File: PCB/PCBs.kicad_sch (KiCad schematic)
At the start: 8 parts, among them U1 ADS1299IPAGR

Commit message: dvdd clk and clksel
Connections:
- net at U2.21 (GP16): now also U1.34 (DIN)
- net at U2.22 (GP17): now also U1.39 (*CS)
- net at U2.24 (GP18): now also U1.40 (SCLK)
- net at U2.25 (GP19): now also U1.43 (DOUT)
- net DVDD: now reaches U1.48 (DVDD)
- net DVDD: now also U1.50 (DVDD), U1.52 (CLKSEL)
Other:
- note added: "TODO: pull up resistor?"
- moved on the sheet: U2

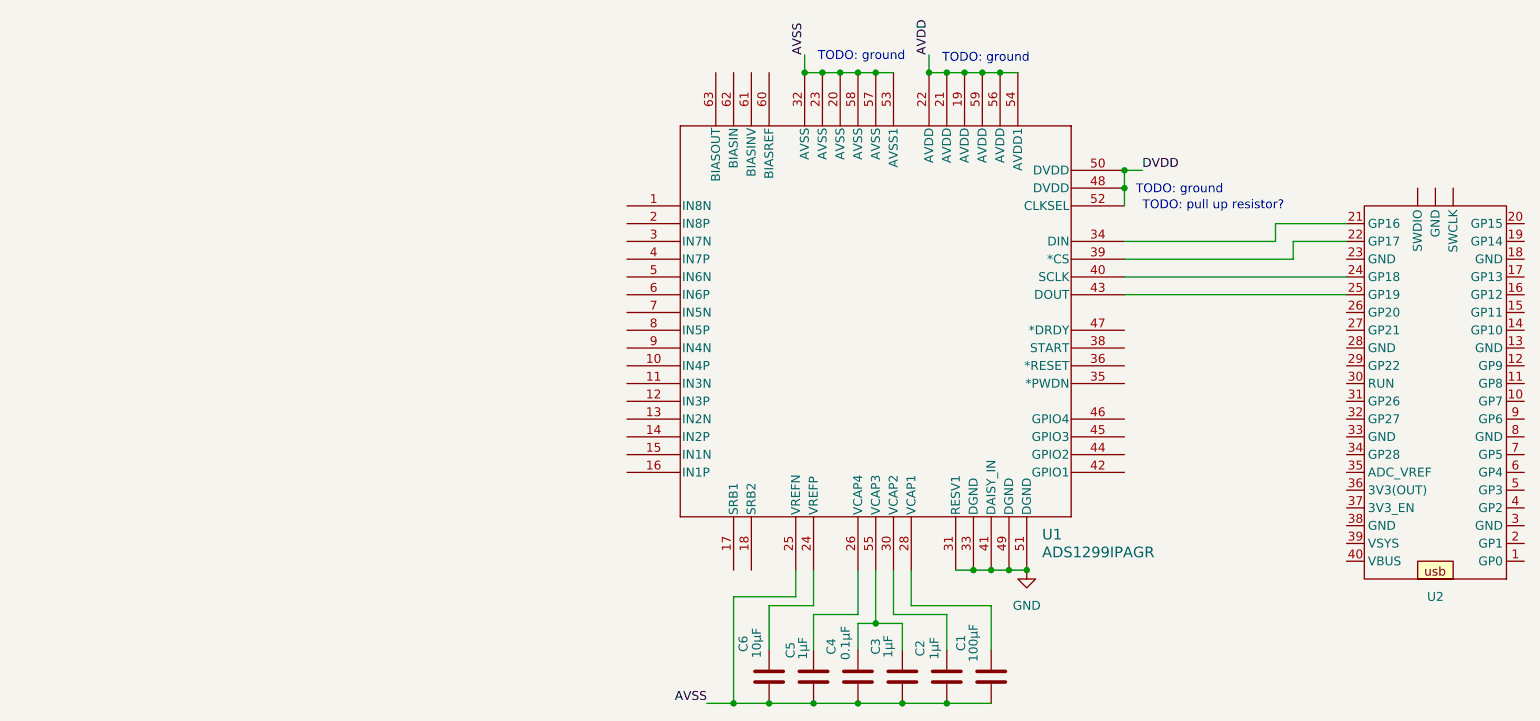
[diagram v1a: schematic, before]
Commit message: first input schem draft
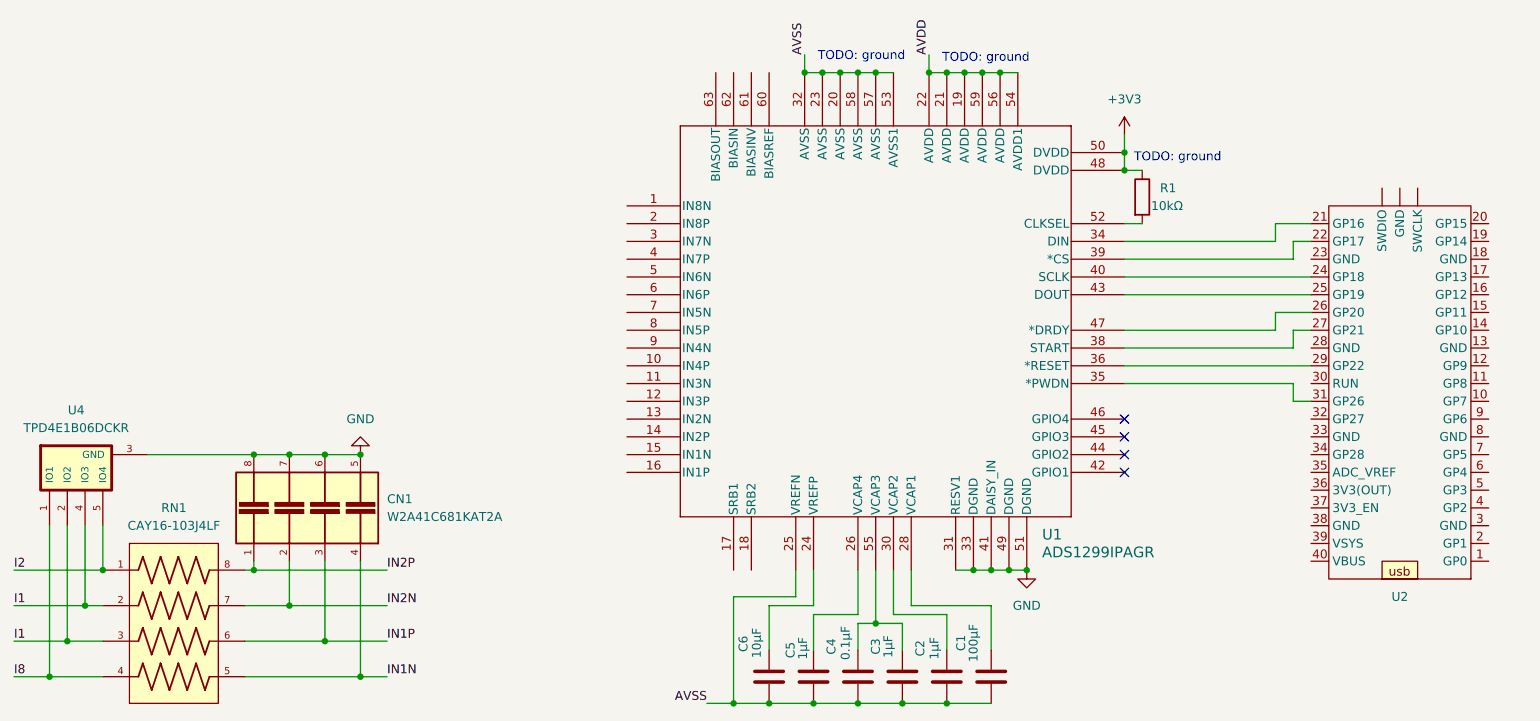
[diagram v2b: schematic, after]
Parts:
- added CN1: W2A41C681KAT2A, W2A41C681KAT2A:CAPCAXE50P210X130X94-8N, symbol custom_lib:W2A41C681KAT2A
- added R1: 10kΩ, symbol Device:R
- added RN1: CAY16-103J4LF, CAY16-103J4LF:RESCAF80P320X160X60-8N, symbol custom_lib:CAY16-103J4LF
- added U4: TPD4E1B06DCKR, TPD4E1B06DCKR:SOT65P210X110-6N, symbol custom_lib:TPD4E1B06DCKR
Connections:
- net GND: now also CN1.5, CN1.6, CN1.7, CN1.8, U4.3 (GND)
- net at U2.26 (GP20): now also U1.47 (*DRDY)
- net at U2.27 (GP21): now also U1.38 (START)
- net at U2.29 (GP22): now also U1.36 (*RESET)
- net at U2.31 (GP26): now also U1.35 (*PWDN)
- net DVDD renamed +3V3
- net +3V3: now also R1.1; no longer U1.52 (CLKSEL)
- new net: R1.2, U1.52 (CLKSEL)
- new net I1: RN1.2, RN1.3, U4.2 (IO2), U4.4 (IO3)
- new net I2: RN1.1, U4.5 (IO4)
- new net I8: RN1.4, U4.1 (IO1)
- new net IN1N: CN1.4, RN1.5
- new net IN1P: CN1.3, RN1.6
- new net IN2N: CN1.2, RN1.7
- new net IN2P: CN1.1, RN1.8
- no-connect marks 0 -> 4
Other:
- note removed: "TODO: pull up resistor?"
- moved on the sheet: U2

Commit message: input cp
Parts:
- added CN2, CN3, CN4: W2A41C681KAT2A, W2A41C681KAT2A:CAPCAXE50P210X130X94-8N, symbol custom_lib:W2A41C681KAT2A
- added RN2, RN3, RN4: CAY16-103J4LF, CAY16-103J4LF:RESCAF80P320X160X60-8N, symbol custom_lib:CAY16-103J4LF
- added U3, U5, U6: TPD4E1B06DCKR, TPD4E1B06DCKR:SOT65P210X110-6N, symbol custom_lib:TPD4E1B06DCKR
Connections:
- net GND: now also CN2.5, CN2.6, CN2.7, CN2.8, CN3.5, CN3.6, CN3.7, CN3.8, CN4.5, CN4.6, CN4.7, CN4.8, U3.3 (GND), U5.3 (GND), U6.3 (GND)
- net I2: now also RN2.4, U3.1 (IO1)
- net I8: now also RN4.1, U6.5 (IO4)
- new net I3: RN2.2, RN2.3, U3.2 (IO2), U3.4 (IO3)
- new net I4: RN2.1, RN3.4, U3.5 (IO4), U5.1 (IO1)
- new net I5: RN3.2, RN3.3, U5.2 (IO2), U5.4 (IO3)
- new net I6: RN3.1, RN4.4, U5.5 (IO4), U6.1 (IO1)
- new net I7: RN4.2, RN4.3, U6.2 (IO2), U6.4 (IO3)
- new net IN3N: CN2.4, RN2.5
- new net IN3P: CN2.3, RN2.6
- new net IN4N: CN2.2, RN2.7
- new net IN4P: CN2.1, RN2.8
- new net IN5N: CN3.4, RN3.5
- new net IN5P: CN3.3, RN3.6
- new net IN6N: CN3.2, RN3.7
- new net IN6P: CN3.1, RN3.8
- new net IN7N: CN4.4, RN4.5
- new net IN7P: CN4.3, RN4.6
- new net IN8N: CN4.2, RN4.7
- new net IN8P: CN4.1, RN4.8
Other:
- moved on the sheet: C1, C2, C3, C4, C5, C6, CN1, R1, RN1, U1, U2, U4

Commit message: input offset montage
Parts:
- removed U3: TPD4E1B06DCKR, TPD4E1B06DCKR:SOT65P210X110-6N, symbol custom_lib:TPD4E1B06DCKR
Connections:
- net GND: now also CN2.1, CN2.2, CN2.3, CN2.4; no longer CN2.5, CN2.6, CN2.7, CN2.8
- net I1: no longer U4.2 (IO2)
- net I2: now also U4.2 (IO2); no longer U4.5 (IO4)
- net I3: now also U4.1 (IO1)
- net I8: now also U4.5 (IO4); no longer U4.1 (IO1)
- net IN3N: now also CN2.8; no longer CN2.4
- net IN3P: now also CN2.7; no longer CN2.3
- net IN4N: now also CN2.6; no longer CN2.2
- net IN4P: now also CN2.5; no longer CN2.1
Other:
- moved on the sheet: CN1, CN2, CN3, CN4, RN1, RN2, RN3, RN4, U5, U6

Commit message: duplicate input
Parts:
- removed CN3: W2A41C681KAT2A, W2A41C681KAT2A:CAPCAXE50P210X130X94-8N, symbol custom_lib:W2A41C681KAT2A
- removed RN3: CAY16-103J4LF, CAY16-103J4LF:RESCAF80P320X160X60-8N, symbol custom_lib:CAY16-103J4LF
- removed U5: TPD4E1B06DCKR, TPD4E1B06DCKR:SOT65P210X110-6N, symbol custom_lib:TPD4E1B06DCKR
- added CN5, CN6: W2A41C681KAT2A, W2A41C681KAT2A:CAPCAXE50P210X130X94-8N, symbol custom_lib:W2A41C681KAT2A
- added RN5, RN6: CAY16-103J4LF, CAY16-103J4LF:RESCAF80P320X160X60-8N, symbol custom_lib:CAY16-103J4LF
- added U3: TPD4E1B06DCKR, TPD4E1B06DCKR:SOT65P210X110-6N, symbol custom_lib:TPD4E1B06DCKR
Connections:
- net GND: now also CN5.1, CN5.2, CN5.3, CN5.4, CN6.5, CN6.6, CN6.7, CN6.8, U3.3 (GND)
- net I4: now also RN6.4, U3.5 (IO4)
- net I5: now also RN6.2, RN6.3, U3.4 (IO3)
- net I6: now also RN5.4, RN6.1, U3.2 (IO2)
- net I7: now also RN5.2, RN5.3, U3.1 (IO1)
- net I8: now also RN5.1
- net IN5N: now also CN6.4, RN6.5
- net IN5P: now also CN6.3, RN6.6
- net IN6N: now also CN6.2, RN6.7
- net IN6P: now also CN6.1, RN6.8
- net IN7N: now also CN5.8, RN5.5
- net IN7P: now also CN5.7, RN5.6
- net IN8N: now also CN5.6, RN5.7
- net IN8P: now also CN5.5, RN5.8
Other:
- moved on the sheet: CN1, CN2, CN4, RN1, RN2, RN4, U4, U6

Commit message: bias input draft
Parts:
- removed CN5: W2A41C681KAT2A, W2A41C681KAT2A:CAPCAXE50P210X130X94-8N, symbol custom_lib:W2A41C681KAT2A
- added C7: C, symbol Device:C
- added C8: 1.5nF, symbol Device:C
- added CN3: W2A41C681KAT2A, W2A41C681KAT2A:CAPCAXE50P210X130X94-8N, symbol custom_lib:W2A41C681KAT2A
- added D1: TPD1E05U06DPYR, TPD1E05U06DPYR:DIO_TPD1E05U06DPYR, symbol custom_lib:TPD1E05U06DPYR
- added R2: R, symbol Device:R
- added R3: 1MΩ, symbol Device:R
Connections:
- net AVSS: now also U1.17 (SRB1), U1.18 (SRB2), U1.60 (BIASREF)
- net GND: now also C7.1, CN3.1, CN3.2, CN3.3, CN3.4, D1.2 (GND)
- net IN1N: now also U1.15 (IN1N)
- net IN1P: now also U1.16 (IN1P)
- net IN2N: now also U1.13 (IN2N)
- net IN2P: now also U1.14 (IN2P)
- net IN3N: now also U1.11 (IN3N)
- net IN3P: now also U1.12 (IN3P)
- net IN4N: now also U1.9 (IN4N)
- net IN4P: now also U1.10 (IN4P)
- net IN5N: now also U1.7 (IN5N)
- net IN5P: now also U1.8 (IN5P)
- net IN6N: now also U1.5 (IN6N)
- net IN6P: now also U1.6 (IN6P)
- net IN7N: now also U1.3 (IN7N), CN3.8
- net IN7P: now also U1.4 (IN7P), CN3.7
- net IN8N: now also U1.1 (IN8N), CN3.6
- net IN8P: now also U1.2 (IN8P), CN3.5
- net at U1.61 (BIASINV): now also C8.1, R3.1
- net Bias: now reaches U1.62 (BIASIN)
- net Bias: now also U1.63 (BIASOUT), C7.2, C8.2, R2.1, R3.2
- new net IB: D1.1 (I/O), R2.2
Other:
- note added: "TODO: AVSS or GND?"
- moved on the sheet: C1, C2, C3, C4, C5, C6, CN1, CN2, CN6, R1, RN1, RN2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

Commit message: volt regs
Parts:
- added U5: TPS73225DBVR, TPS73225DBVR:SOT95P280X145-5N, symbol custom_lib:TPS73225DBVR
- added U7: LM2664M6, LM2664M6:SOT95P300X120-6N, symbol custom_lib:LM2664M6
- added U8: TPS73233DBVT, TPS73233DBVT:SOT95P280X145-5N, symbol custom_lib:TPS73233DBVT
- added U9: TPS72325DBVT, TPS72325DBVT:SOT95P280X145-5N, symbol custom_lib:TPS72325DBVT
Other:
- note added: "TODO: +0.1uF"
- note added: "TODO: GND P64"
- note added: "TODO: pull resistors"
- note added: "TODO: verify"

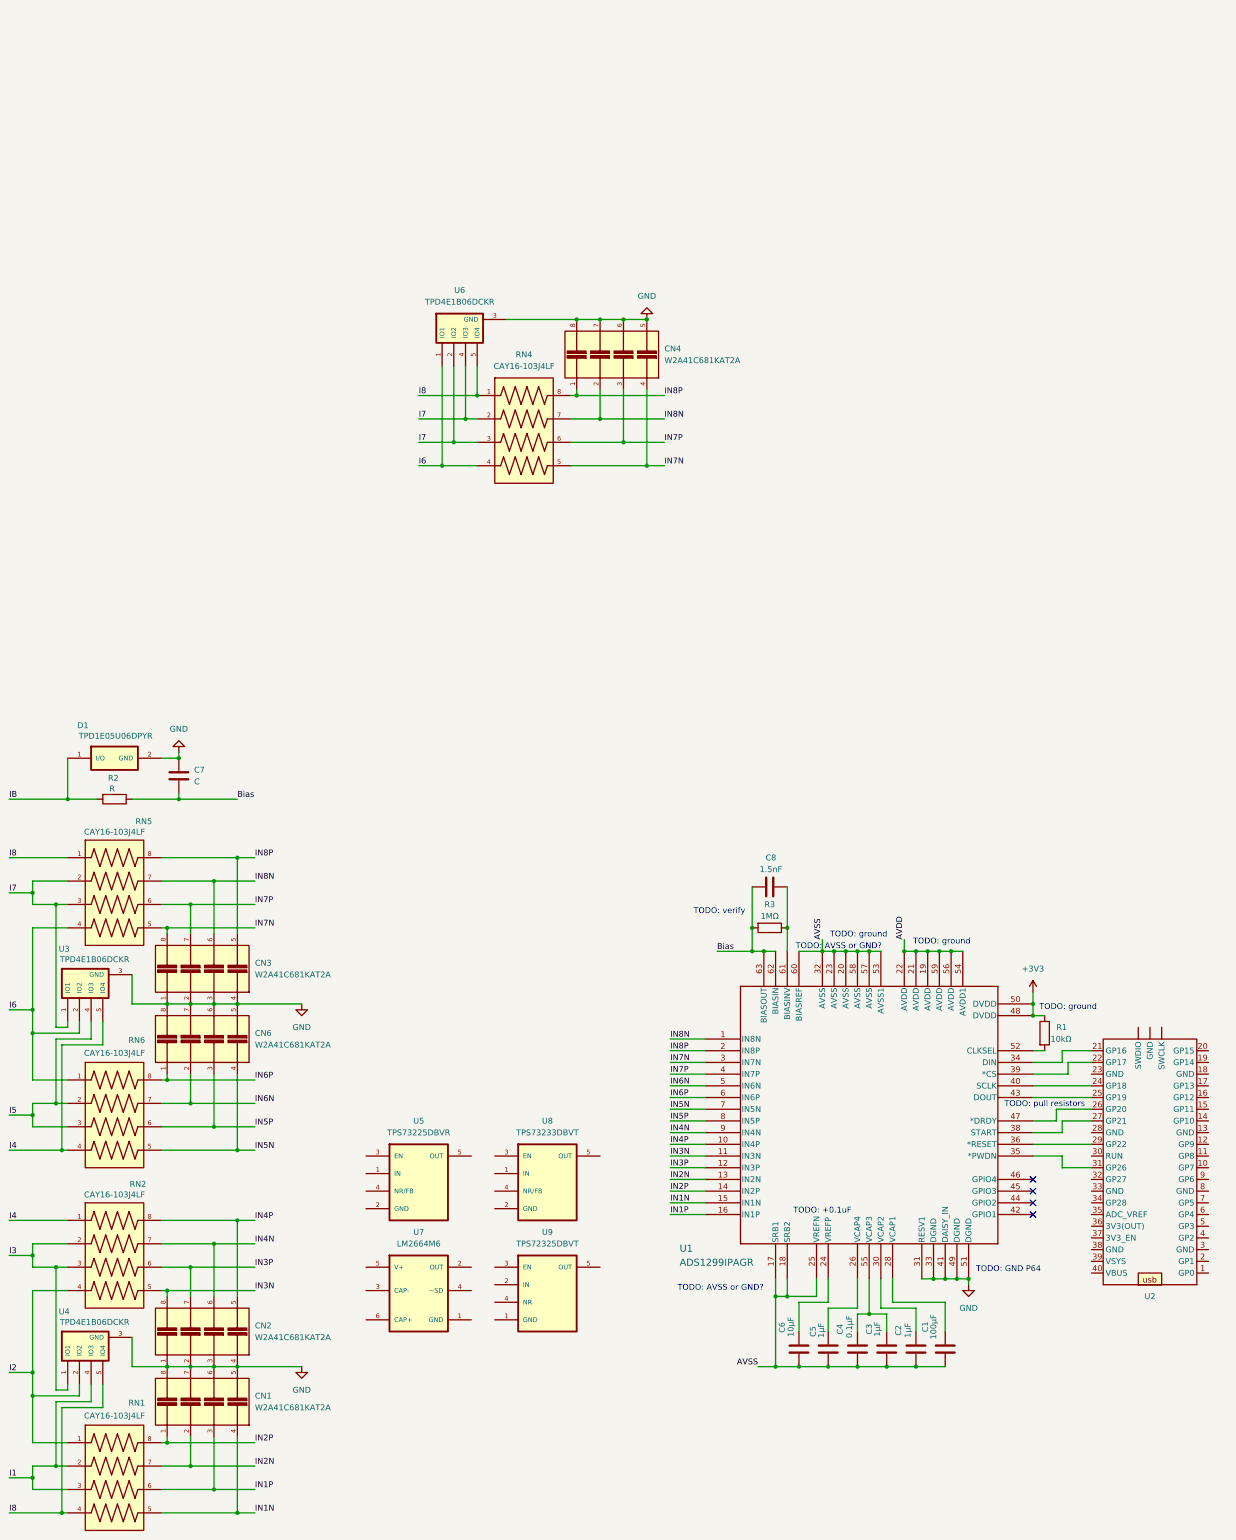
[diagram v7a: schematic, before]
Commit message: booster and voltage regulators
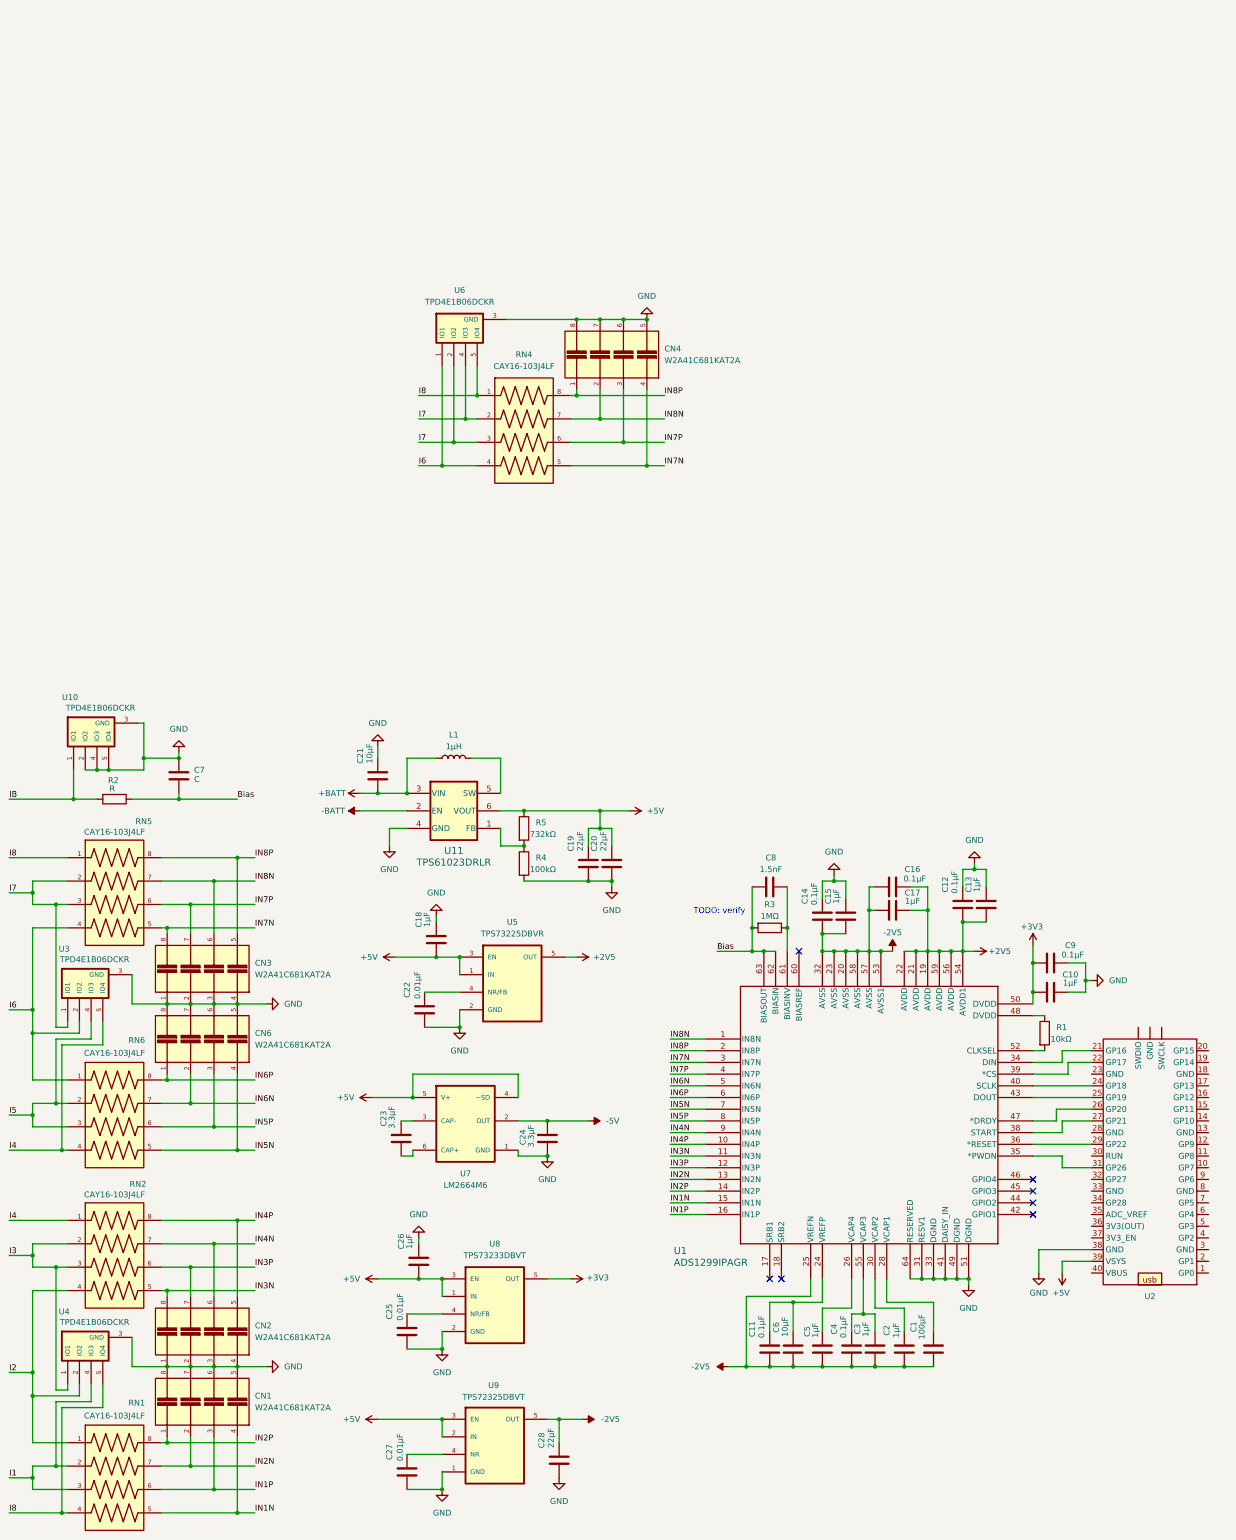
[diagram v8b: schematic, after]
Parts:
- removed D1: TPD1E05U06DPYR, TPD1E05U06DPYR:DIO_TPD1E05U06DPYR, symbol custom_lib:TPD1E05U06DPYR
- added C10, C13, C15, C17, C18, C26: 1µF, symbol Device:C
- added C11, C12, C14, C16, C9: 0.1µF, symbol Device:C
- added C19, C20, C28: 22µF, symbol Device:C
- added C21: 10µF, symbol Device:C
- added C22, C25, C27: 0.01µF, symbol Device:C
- added C23, C24: 3.3µF, symbol Device:C
- added L1: 1µH, symbol Device:L
- added R4: 100kΩ, symbol Device:R
- added R5: 732kΩ, symbol Device:R
- added U10: TPD4E1B06DCKR, TPD4E1B06DCKR:SOT65P210X110-6N, symbol custom_lib:TPD4E1B06DCKR
- added U11: TPS61023DRLR, DRL0006A, symbol custom_lib:TPS61023DRLR
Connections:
- net AVDD is gone; now on net +2V5: U1.19 (AVDD), U1.21 (AVDD), U1.22 (AVDD), U1.54 (AVDD1), U1.56 (AVDD), U1.59 (AVDD)
- net +3V3: now also U8.5 (OUT), C10.1, C9.1; no longer R1.1, U1.48 (DVDD)
- net GND: now also U1.64 (RESERVED), U2.38 (GND), U5.2 (GND), U7.1 (GND), U8.2 (GND), U9.1 (GND), C10.2, C12.2, C13.2, C14.2, C15.2, C18.2, C19.1, C20.1, C21.2, C22.1, C24.1, C25.1, C26.2, C27.1, C28.1, C9.2, R4.2, U10.2 (IO2), U10.3 (GND), U10.4 (IO3), U10.5 (IO4), U11.4 (GND)
- net IB: now also U10.1 (IO1)
- net +5V: now reaches U9.2 (IN)
- net +5V: now also U2.39 (VSYS), U5.1 (IN), U5.3 (EN), U7.4 (~SD), U7.5 (V+), U8.1 (IN), U8.3 (EN), U9.3 (EN), C18.1, C19.2, C20.2, C26.1, R5.1, U11.6 (VOUT)
- net at U9.4 (NR): now also C27.2
- net -2V5: now reaches U9.5 (OUT)
- net -2V5: now also C1.2, C2.2, C3.1, C4.1, C5.2, C6.2, U1.20 (AVSS), U1.23 (AVSS), U1.25 (VREFN), U1.32 (AVSS), U1.53 (AVSS1), U1.57 (AVSS), U1.58 (AVSS), C11.1, C14.1, C15.1, C16.1, C17.1, C28.2
- net at U5.4 (NR/FB): now also C22.2
- net +2V5: now reaches U5.5 (OUT)
- net +2V5: now also C12.1, C13.1, C16.2, C17.2
- net -5V: now reaches U7.2 (OUT)
- net -5V: now also C24.2
- net at U7.3 (CAP-): now also C23.2
- net at U7.6 (CAP+): now also C23.1
- net at U8.4 (NR/FB): now also C25.2
- net at C6.1, U1.24 (VREFP): now also C11.2
- removed net AVSS: C1.2, C2.2, C3.1, C4.1, C5.2, C6.2, U1.17 (SRB1), U1.18 (SRB2), U1.20 (AVSS), U1.23 (AVSS), U1.25 (VREFN), U1.32 (AVSS), U1.53 (AVSS1), U1.57 (AVSS), U1.58 (AVSS), U1.60 (BIASREF)
- new net: L1.2, U11.5 (SW)
- new net: R4.1, R5.2, U11.1 (FB)
- new net: R1.1, U1.48 (DVDD)
- new net +BATT: C21.1, L1.1, U11.3 (VIN)
- new net -BATT: U11.2 (EN)
- no-connect marks 4 -> 7
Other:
- note removed: "TODO: +0.1uF"
- note removed: "TODO: AVSS or GND?"
- note removed: "TODO: GND P64"
- note removed: "TODO: ground"
- note removed: "TODO: pull resistors"
- moved on the sheet: C1, C2, C3, C4, C5, C6, U5, U8, U9
